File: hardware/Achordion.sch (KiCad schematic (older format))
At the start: 98 parts, among them J1 Power, J10 Jack, J11 Jack, J4 Jack, J5 Jack, J6 Jack, J7 Jack, J8 Jack, J9 Jack, SW2 Button, U4 LM4040C10, U6 TL072, U7 MCP6002, U8 MCP6002, U9 MCP6002

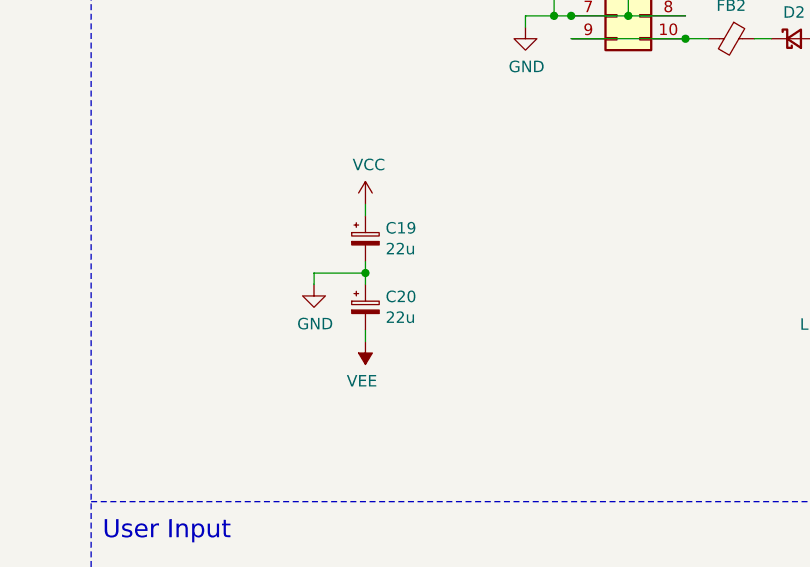
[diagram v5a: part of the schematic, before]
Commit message: Use 10uF for decoupling caps
This value seems to be more common in stores. It should not matter if 22
or 10 is used, so let's go with the common one.

Signed-off-by: Petr Horacek <hrck@protonmail.com>
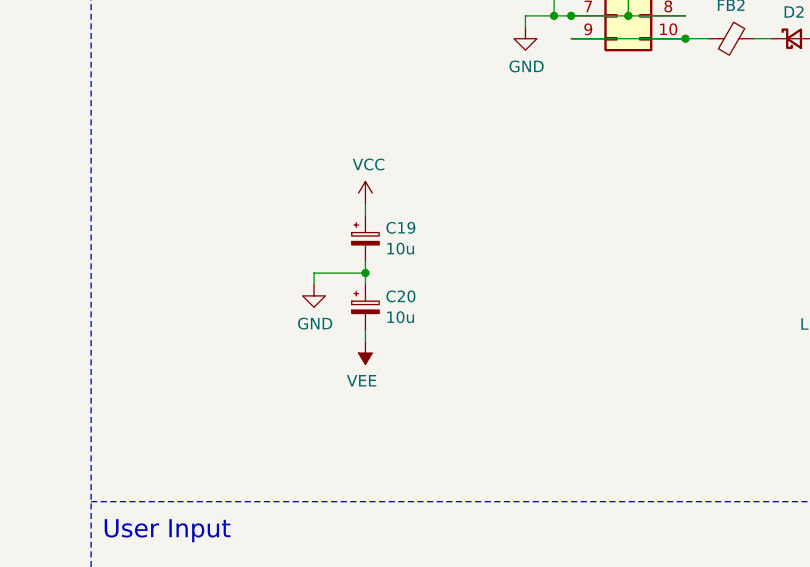
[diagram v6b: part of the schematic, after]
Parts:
- C19, C20: value 22u -> 10u
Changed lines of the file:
@@
 P 12275 2750
 F 0 "C20" H 12363 2796 50  0000 L CNN
-F 1 "22u" H 12363 2705 50  0000 L CNN
+F 1 "10u" H 12363 2705 50  0000 L CNN
 F 2 "Capacitor_SMD:CP_Elec_6.3x5.8" H 12275 2750 50  0001 C CNN
 F 3 "~" H 12275 2750 50  0001 C CNN
@@
 P 12275 2450
 F 0 "C19" H 12363 2496 50  0000 L CNN
-F 1 "22u" H 12363 2405 50  0000 L CNN
+F 1 "10u" H 12363 2405 50  0000 L CNN
 F 2 "Capacitor_SMD:CP_Elec_6.3x5.8" H 12275 2450 50  0001 C CNN
 F 3 "~" H 12275 2450 50  0001 C CNN

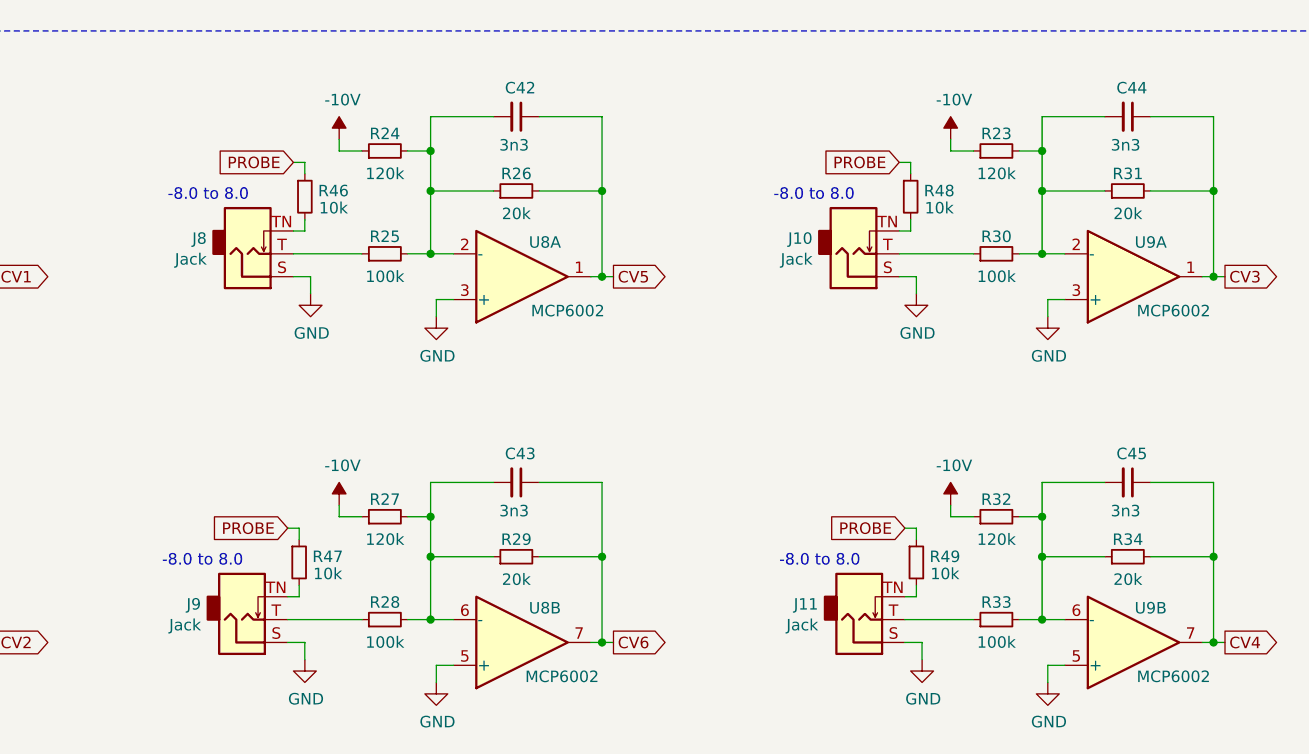
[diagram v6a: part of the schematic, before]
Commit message: Scale down input CV to -5 to +5 V
This seems to be slightly more common than -8 to +8 V, it would allow
narrower CV source to control the value from one end to the other and it
adheres to unwritten 10 Vpp standard.

Signed-off-by: Petr Horacek <hrck@protonmail.com>
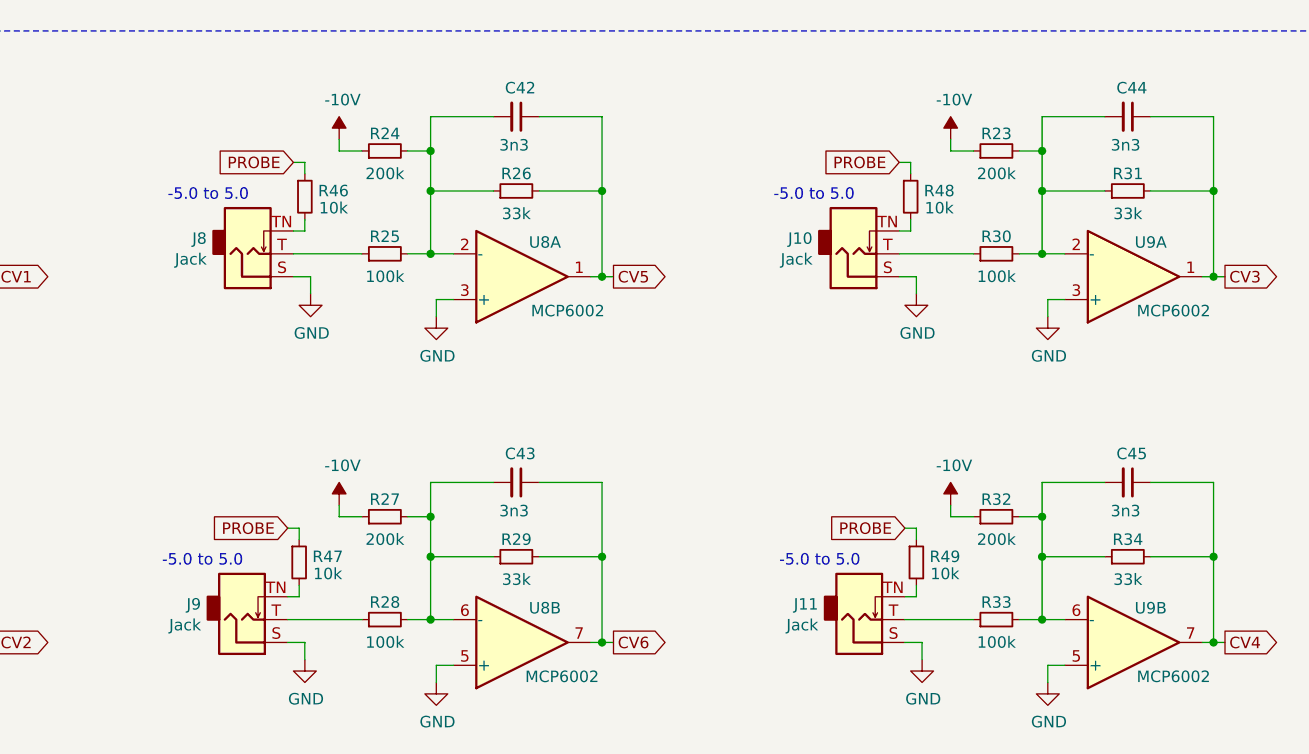
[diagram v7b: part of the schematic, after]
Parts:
- R23, R24, R27, R32: value 120k -> 200k
- R26, R29, R31, R34: value 20k -> 33k
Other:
- note added: "-5.0 to 5.0"
- note removed: "-8.0 to 8.0"
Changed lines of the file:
@@
 P 7125 7475
 F 0 "R23" V 7200 7475 50  0000 C CNN
-F 1 "120k" V 7025 7475 50  0000 C CNN
+F 1 "200k" V 7025 7475 50  0000 C CNN
 F 2 "Resistor_SMD:R_0603_1608Metric_Pad0.98x0.95mm_HandSolder" H 7125 7475 50  0001 C CNN
 F 3 "~" H 7125 7475 50  0001 C CNN
@@
 P 7700 7650
 F 0 "R31" V 7775 7650 50  0000 C CNN
-F 1 "20k" V 7600 7650 50  0000 C CNN
+F 1 "33k" V 7600 7650 50  0000 C CNN
 F 2 "Resistor_SMD:R_0603_1608Metric_Pad0.98x0.95mm_HandSolder" H 7700 7650 50  0001 C CNN
 F 3 "~" H 7700 7650 50  0001 C CNN
@@
 P 7125 9075
 F 0 "R32" V 7200 9075 50  0000 C CNN
-F 1 "120k" V 7025 9075 50  0000 C CNN
+F 1 "200k" V 7025 9075 50  0000 C CNN
 F 2 "Resistor_SMD:R_0603_1608Metric_Pad0.98x0.95mm_HandSolder" H 7125 9075 50  0001 C CNN
 F 3 "~" H 7125 9075 50  0001 C CNN
@@
 P 7700 9250
 F 0 "R34" V 7775 9250 50  0000 C CNN
-F 1 "20k" V 7600 9250 50  0000 C CNN
+F 1 "33k" V 7600 9250 50  0000 C CNN
 F 2 "Resistor_SMD:R_0603_1608Metric_Pad0.98x0.95mm_HandSolder" H 7700 9250 50  0001 C CNN
 F 3 "~" H 7700 9250 50  0001 C CNN
@@
 P 5025 7650
 F 0 "R26" V 5100 7650 50  0000 C CNN
-F 1 "20k" V 4925 7650 50  0000 C CNN
+F 1 "33k" V 4925 7650 50  0000 C CNN
 F 2 "Resistor_SMD:R_0603_1608Metric_Pad0.98x0.95mm_HandSolder" H 5025 7650 50  0001 C CNN
 F 3 "~" H 5025 7650 50  0001 C CNN
@@
 P 4450 7475
 F 0 "R24" V 4525 7475 50  0000 C CNN
-F 1 "120k" V 4350 7475 50  0000 C CNN
+F 1 "200k" V 4350 7475 50  0000 C CNN
 F 2 "Resistor_SMD:R_0603_1608Metric_Pad0.98x0.95mm_HandSolder" H 4450 7475 50  0001 C CNN
 F 3 "~" H 4450 7475 50  0001 C CNN
@@
 P 5025 9250
 F 0 "R29" V 5100 9250 50  0000 C CNN
-F 1 "20k" V 4925 9250 50  0000 C CNN
+F 1 "33k" V 4925 9250 50  0000 C CNN
 F 2 "Resistor_SMD:R_0603_1608Metric_Pad0.98x0.95mm_HandSolder" H 5025 9250 50  0001 C CNN
 F 3 "~" H 5025 9250 50  0001 C CNN
@@
 P 4450 9075
 F 0 "R27" V 4525 9075 50  0000 C CNN
-F 1 "120k" V 4350 9075 50  0000 C CNN
+F 1 "200k" V 4350 9075 50  0000 C CNN
 F 2 "Resistor_SMD:R_0603_1608Metric_Pad0.98x0.95mm_HandSolder" H 4450 9075 50  0001 C CNN
 F 3 "~" H 4450 9075 50  0001 C CNN
@@
 $EndComp
 Text Notes 3475 9300 0    50   ~ 0
--8.0 to 8.0
+-5.0 to 5.0
 Text GLabel 5450 9625 2    50   Output ~ 0
 CV6
@@
 $EndComp
 Text Notes 3500 7700 0    50   ~ 0
--8.0 to 8.0
+-5.0 to 5.0
 $Comp
 L Connector:AudioJack2_SwitchT J8
@@
 PROBE
 Text Notes 6150 7700 0    50   ~ 0
--8.0 to 8.0
+-5.0 to 5.0
 $Comp
 L power:GND #PWR079
@@
 PROBE
 Text Notes 6175 9300 0    50   ~ 0
--8.0 to 8.0
+-5.0 to 5.0
 $Comp
 L power:GND #PWR082

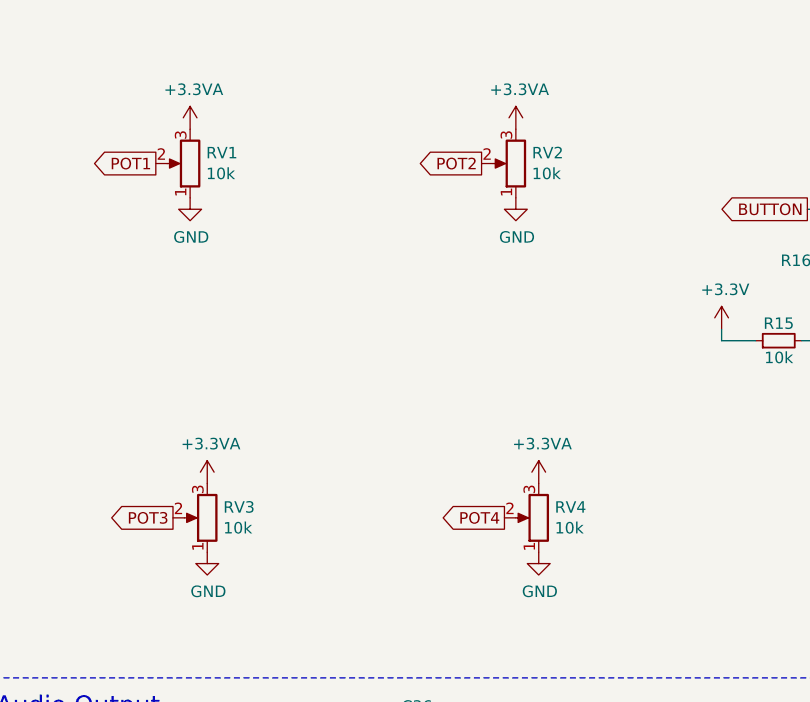
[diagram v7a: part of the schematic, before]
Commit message: Add assembly labels for pots and leds
Signed-off-by: Petr Horacek <hrck@protonmail.com>
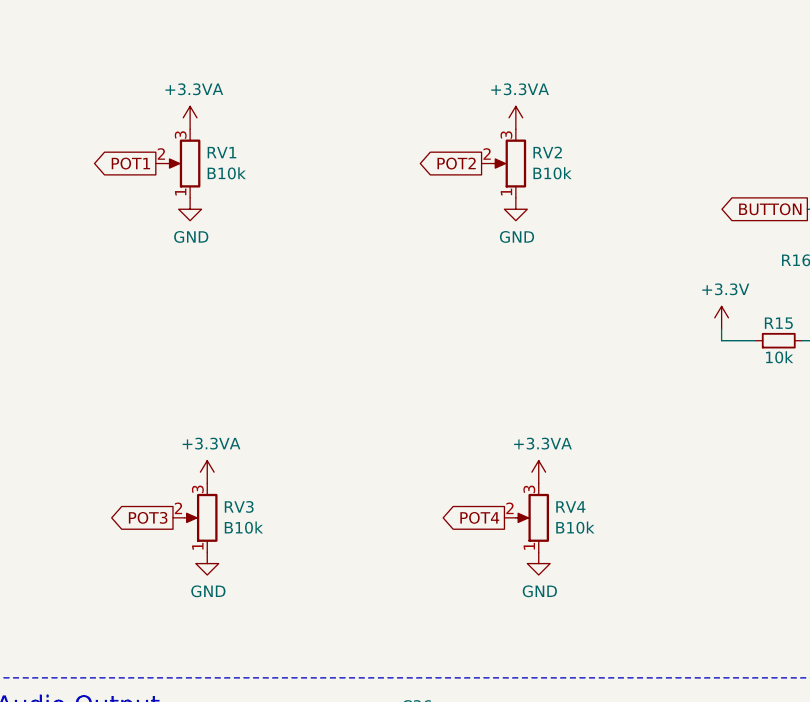
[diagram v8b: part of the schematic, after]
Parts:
- RV1, RV2, RV3, RV4: value 10k -> B10k
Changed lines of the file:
@@
 P 13525 6250
 F 0 "RV4" H 13455 6204 50  0000 R CNN
-F 1 "10k" H 13455 6295 50  0000 R CNN
+F 1 "B10k" H 13455 6295 50  0000 R CNN
 F 2 "Potentiometer_THT:Potentiometer_Alps_RK09L_Single_Vertical" H 13525 6250 50  0001 C CNN
 F 3 "~" H 13525 6250 50  0001 C CNN
@@
 P 13425 4700
 F 0 "RV2" H 13355 4654 50  0000 R CNN
-F 1 "10k" H 13355 4745 50  0000 R CNN
+F 1 "B10k" H 13355 4745 50  0000 R CNN
 F 2 "Potentiometer_THT:Potentiometer_Alps_RK09L_Single_Vertical" H 13425 4700 50  0001 C CNN
 F 3 "~" H 13425 4700 50  0001 C CNN
@@
 P 12000 4700
 F 0 "RV1" H 11930 4654 50  0000 R CNN
-F 1 "10k" H 11930 4745 50  0000 R CNN
+F 1 "B10k" H 11930 4745 50  0000 R CNN
 F 2 "Potentiometer_THT:Potentiometer_Alps_RK09L_Single_Vertical" H 12000 4700 50  0001 C CNN
 F 3 "~" H 12000 4700 50  0001 C CNN
@@
 P 12075 6250
 F 0 "RV3" H 12005 6204 50  0000 R CNN
-F 1 "10k" H 12005 6295 50  0000 R CNN
+F 1 "B10k" H 12005 6295 50  0000 R CNN
 F 2 "Potentiometer_THT:Potentiometer_Alps_RK09L_Single_Vertical" H 12075 6250 50  0001 C CNN
 F 3 "~" H 12075 6250 50  0001 C CNN
